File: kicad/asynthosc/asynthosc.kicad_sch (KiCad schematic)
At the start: 0 parts

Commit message: sch: wip
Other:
- sheet Analog_in ports: added CVIN0, CVIN1, CVIN2, CVIN3, TRG0; removed none
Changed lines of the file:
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@@
 	)
 	(sheet
-		(at 95.25 135.89)
+		(at 38.1 123.19)
 		(size 52.07 33.02)
 		(fields_autoplaced yes)
@@
 		)
 		(property "Sheetname" "Analog_in"
-			(at 95.25 135.1784 0)
+			(at 38.1 122.4784 0)
 			(effects
 				(font
@@
 		)
 		(property "Sheetfile" "analog_in.kicad_sch"
-			(at 95.25 169.4946 0)
+			(at 38.1 156.7946 0)
 			(effects
 				(font
@@
 			)
 		)
+		(pin "CVIN1" input
+			(at 90.17 133.35 0)
+			(effects
+				(font
+					(size 1.27 1.27)
+				)
+				(justify right)
+			)
+		)
+		(pin "CVIN2" output
+			(at 90.17 135.89 0)
+			(effects
+				(font
+					(size 1.27 1.27)
+				)
+				(justify right)
+			)
+		)
+		(pin "TRG0" output
+			(at 90.17 142.24 0)
+			(effects
+				(font
+					(size 1.27 1.27)
+				)
+				(justify right)
+			)
+		)
+		(pin "CVIN3" output
+			(at 90.17 138.43 0)
+			(effects
+				(font
+					(size 1.27 1.27)
+				)
+				(justify right)
+			)
+		)
+		(pin "CVIN0" output
+			(at 90.17 130.81 0)
+			(effects
+				(font
+					(size 1.27 1.27)
+				)
+				(justify right)
+			)
+		)

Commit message: sch: rmii side
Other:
- sheet Soc ports: added USB_D_N, USB_D_P, USB_ID, USB_VBUS; removed AIN1
- sheet Supply ports: added USB_ID, USB_VBUS; removed none
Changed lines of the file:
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@@
 	(generator_version "8.0")
 	(paper "A3")
-	(sheet
-		(at 60.96 74.93)
-		(size 50.8 29.21)
+	(wire
+		(pts
+			(xy 111.76 86.36) (xy 127 86.36)
+		)
+		(stroke
+			(width 0)
+			(type default)
+		)
+	)
+	(wire
+		(pts
+			(xy 111.76 81.28) (xy 127 81.28)
+		)
+		(stroke
+			(width 0)
+			(type default)
+		)
+	)
+	(wire
+		(pts
+			(xy 111.76 83.82) (xy 127 83.82)
+		)
+		(stroke
+			(width 0)
+			(type default)
+		)
+	)
+	(wire
+		(pts
+			(xy 111.76 78.74) (xy 127 78.74)
+		)
+		(stroke
+			(width 0)
+			(type default)
+		)
+	)
+	(sheet
+		(at 90.17 74.93)
+		(size 21.59 16.51)
 		(fields_autoplaced yes)
 		(stroke
@@
 		)
 		(property "Sheetname" "Supply"
-			(at 60.96 74.2184 0)
+			(at 90.17 74.2184 0)
 			(effects
 				(font
@@
 		)
 		(property "Sheetfile" "supply.kicad_sch"
-			(at 60.96 104.7246 0)
+			(at 90.17 92.0246 0)
 			(effects
 				(font
@@
 		(pin "USB_DN" input
 			(at 111.76 83.82 0)
+			(effects
+				(font
+					(size 1.27 1.27)
+				)
+				(justify right)
+			)
+		)
+		(pin "USB_VBUS" input
+			(at 111.76 78.74 0)
+			(effects
+				(font
+					(size 1.27 1.27)
+				)
+				(justify right)
+			)
+		)
+		(pin "USB_ID" input
+			(at 111.76 86.36 0)
 			(effects
 				(font
@@
 	)
 	(sheet
-		(at 114.3 176.53)
-		(size 57.15 67.31)
+		(at 127 74.93)
+		(size 49.53 63.5)
 		(fields_autoplaced yes)
 		(stroke
@@
 		)
 		(property "Sheetname" "Soc"
-			(at 114.3 175.8184 0)
+			(at 127 74.2184 0)
 			(effects
 				(font
@@
 		)
 		(property "Sheetfile" "soc.kicad_sch"
-			(at 114.3 244.4246 0)
-			(effects
-				(font
-					(size 1.27 1.27)
-				)
-				(justify left top)
-			)
-		)
-		(pin "AIN1" input
-			(at 114.3 205.74 180)
-			(effects
-				(font
+			(at 127 139.0146 0)
+			(effects
+				(font
+					(size 1.27 1.27)
+				)
+				(justify left top)
+			)
+		)
+		(pin "USB_VBUS" input
+			(at 127 78.74 180)
+			(effects
+				(font
+					(size 1.27 1.27)
+				)
+				(justify left)
+			)
+		)
+		(pin "USB_D_N" bidirectional
+			(at 127 83.82 180)
+			(effects
+				(font
+					(size 1.27 1.27)
+				)
+				(justify left)
+			)
+		)
+		(pin "USB_D_P" bidirectional
+			(at 127 81.28 180)
+			(effects
+				(font
+					(size 1.27 1.27)
+				)
+				(justify left)
+			)
+		)
+		(pin "USB_ID" input
+			(at 127 86.36 180)
+			(effects
+				(font

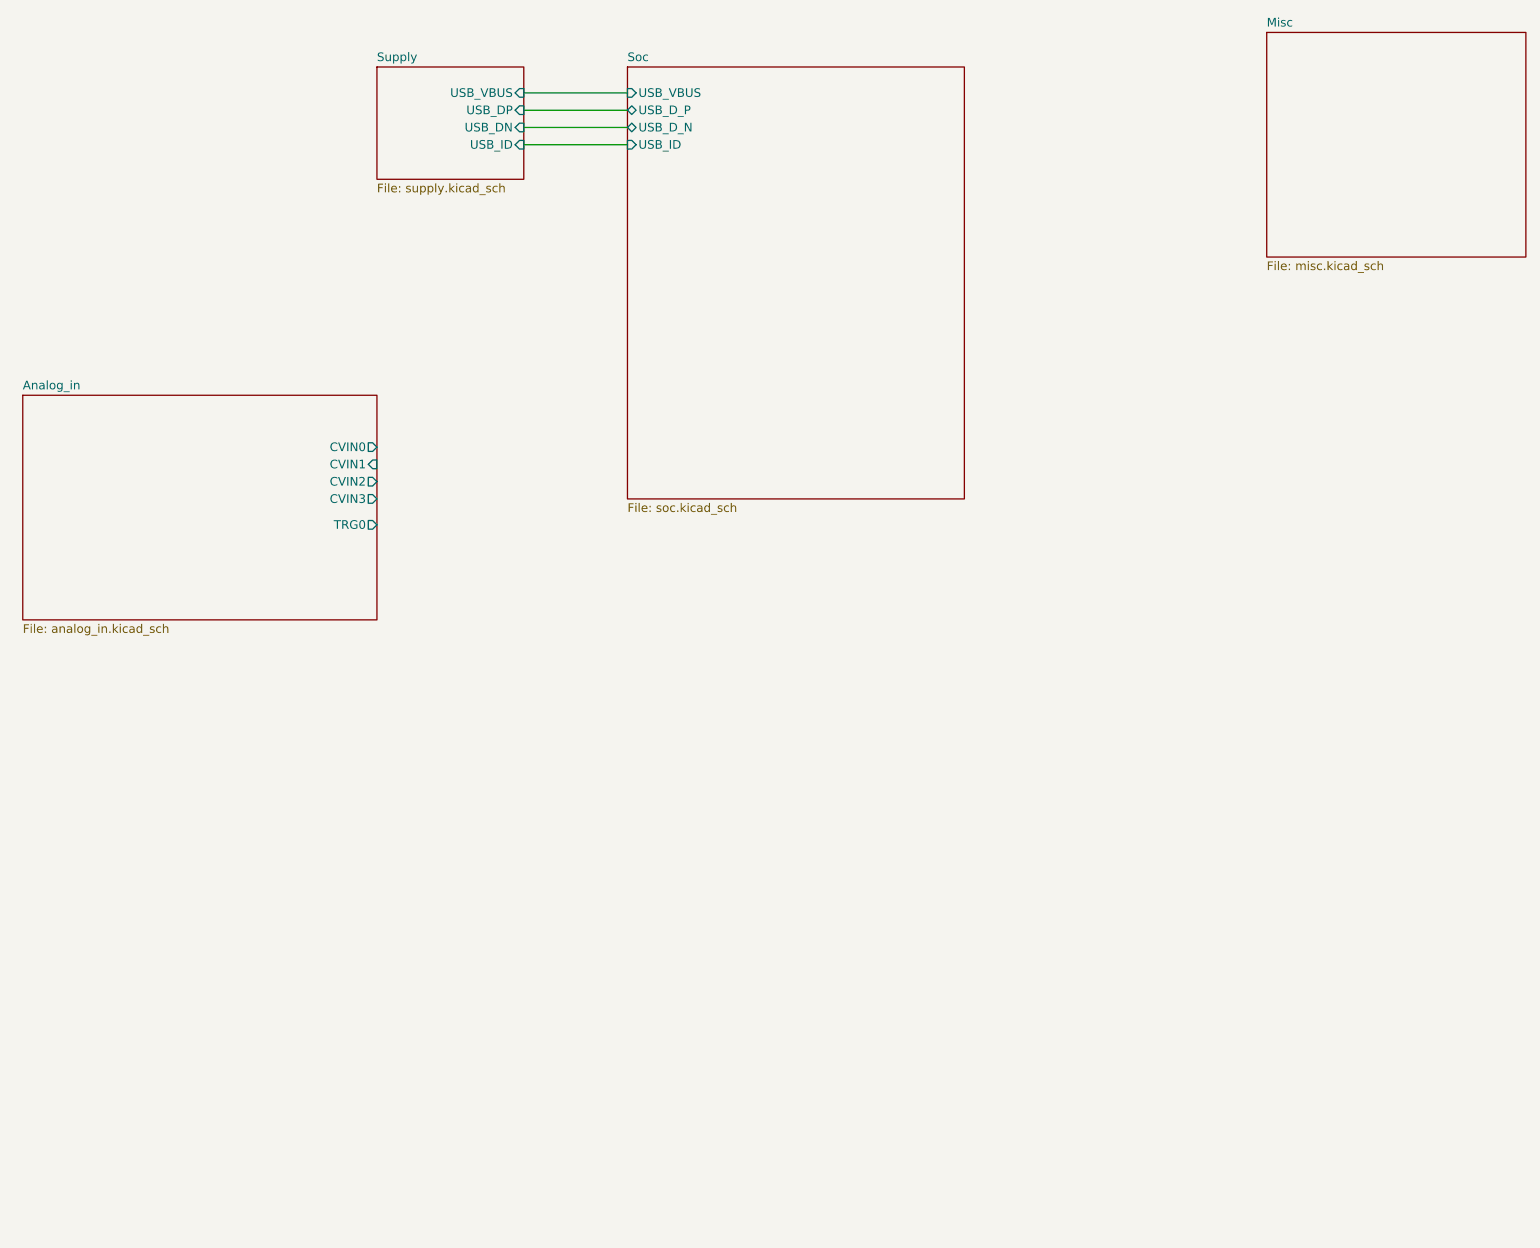
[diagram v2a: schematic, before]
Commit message: sch: top sheet pins input
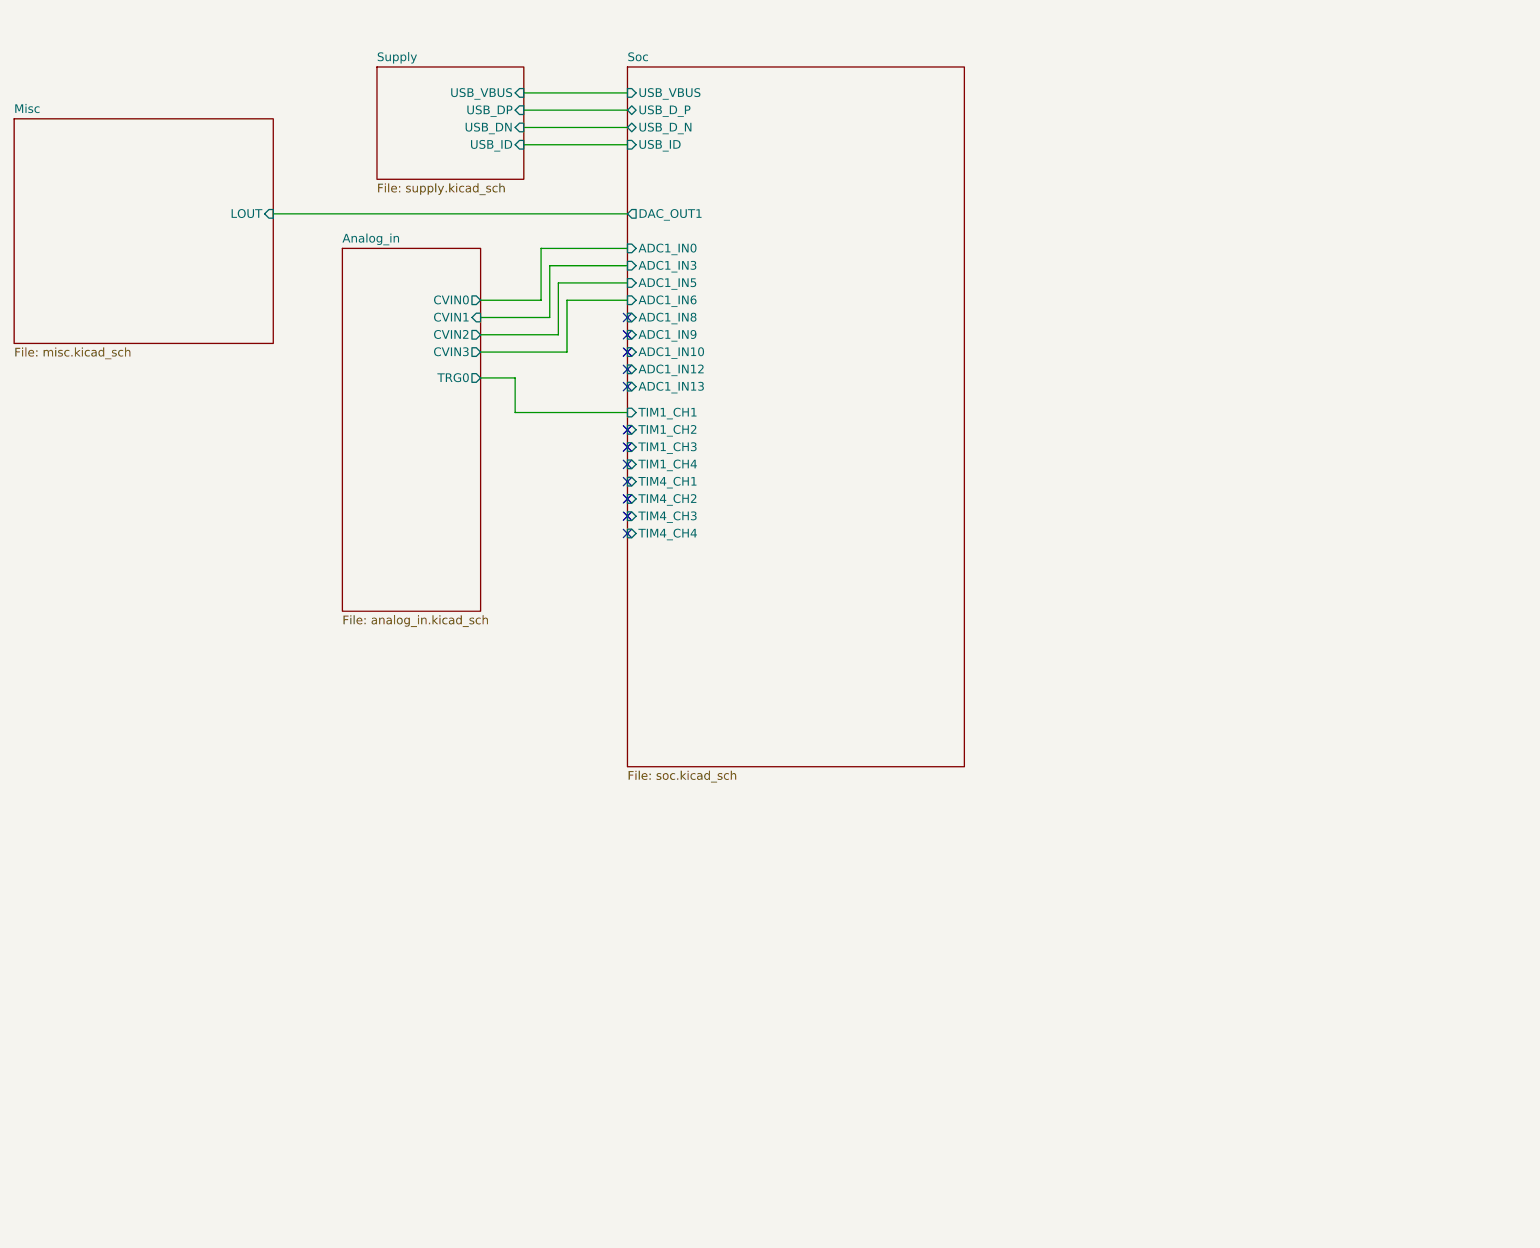
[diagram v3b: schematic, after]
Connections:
- no-connect marks 0 -> 12
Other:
- sheet Misc ports: added LOUT; removed none
- sheet Soc ports: added ADC1_IN0, ADC1_IN10, ADC1_IN12, ADC1_IN13, ADC1_IN3, ADC1_IN5, ADC1_IN6, ADC1_IN8, ADC1_IN9, DAC_OUT1, TIM1_CH1, TIM1_CH2, TIM1_CH3, TIM1_CH4, TIM4_CH1, TIM4_CH2, TIM4_CH3, TIM4_CH4; removed none

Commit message: sch: update and new interface sheet
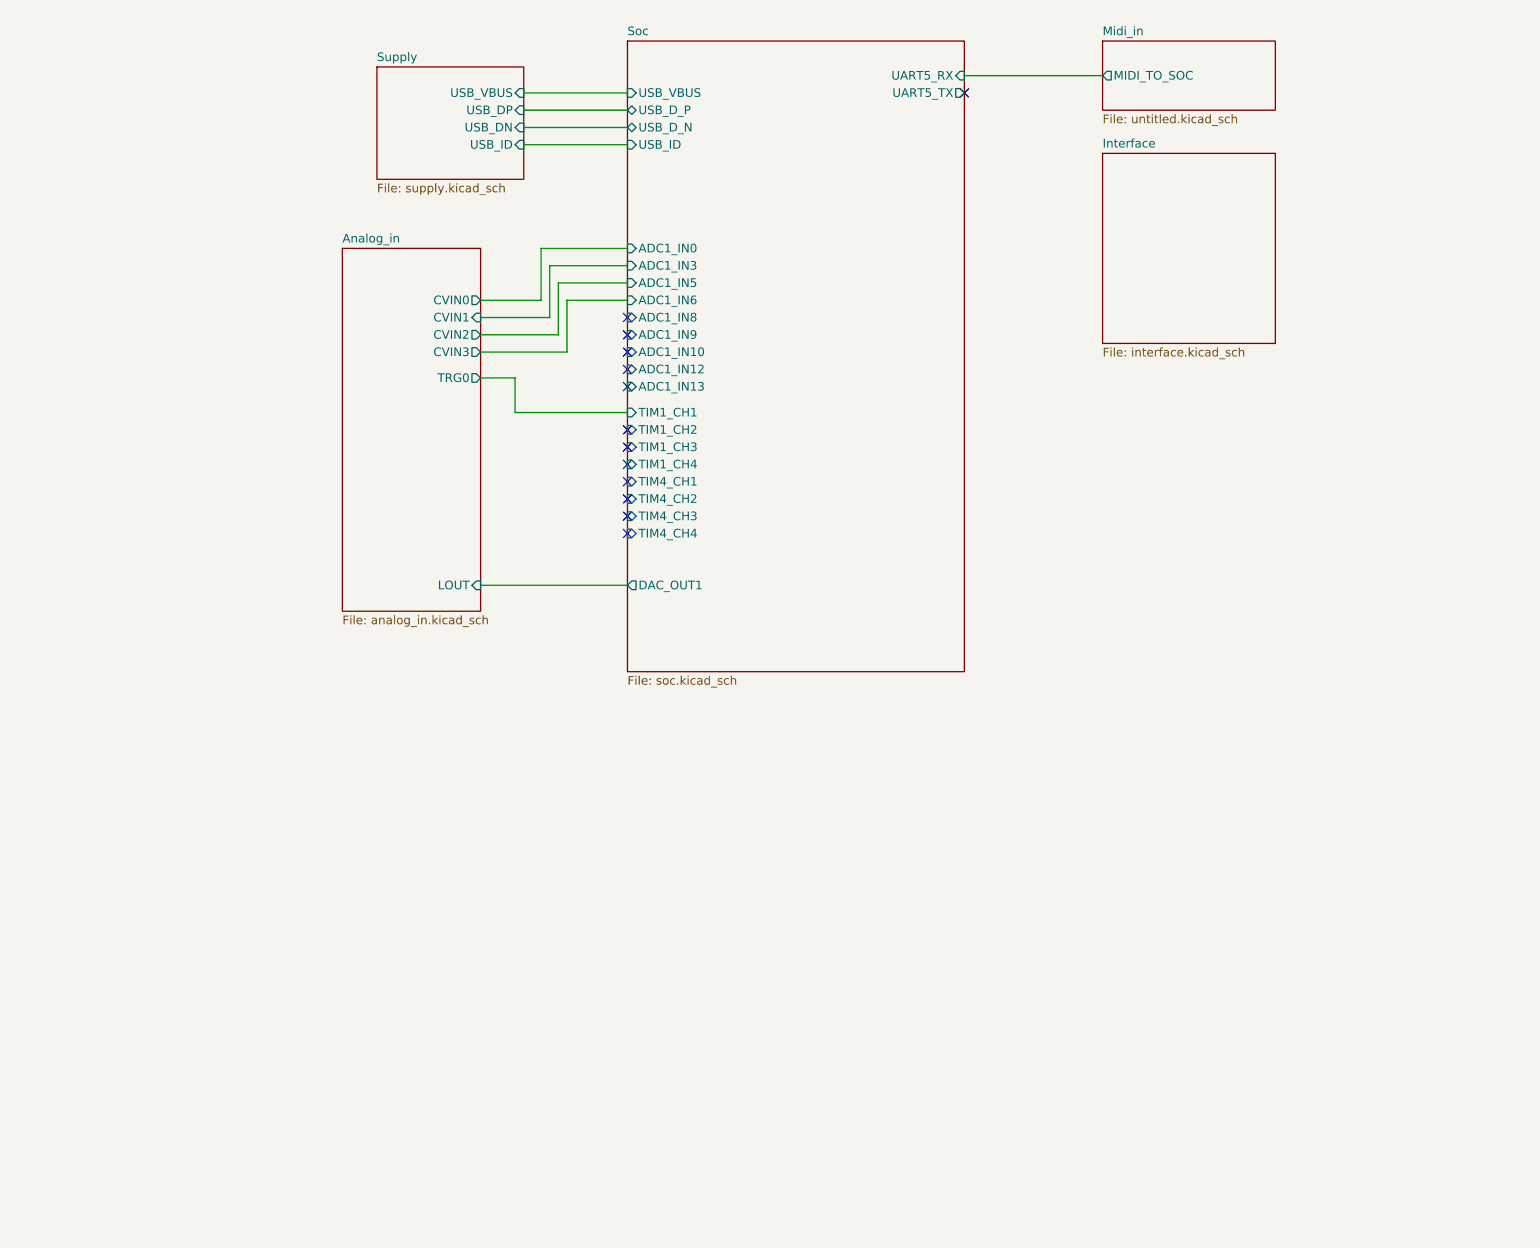
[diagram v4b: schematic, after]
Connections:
- no-connect marks 12 -> 13
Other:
- removed sheet Misc
- added sheet Interface (interface.kicad_sch)
- added sheet Midi_in (untitled.kicad_sch)
- sheet Analog_in ports: added LOUT; removed none
- sheet Soc ports: added UART5_RX, UART5_TX; removed none
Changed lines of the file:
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@@
 		(at 127 128.27)
 	)
-	(wire
-		(pts
-			(xy 74.93 96.52) (xy 127 96.52)
-		)
-		(stroke
-			(width 0)
-			(type default)
-		)
+	(no_connect
+		(at 176.53 78.74)
 	)
 	(wire
@@
 	(wire
 		(pts
+			(xy 176.53 76.2) (xy 196.85 76.2)
+		)
+		(stroke
+			(width 0)
+			(type default)
+		)
+	)
+	(wire
+		(pts
 			(xy 111.76 86.36) (xy 127 86.36)
 		)
@@
 		(pts
 			(xy 105.41 120.65) (xy 110.49 120.65)
+		)
+		(stroke
+			(width 0)
+			(type default)
+		)
+	)
+	(wire
+		(pts
+			(xy 105.41 151.13) (xy 127 151.13)
 		)
 		(stroke
@@
 			)
 		)
+		(pin "LOUT" input
+			(at 105.41 151.13 0)
+			(effects
+				(font
+					(size 1.27 1.27)
+				)
+				(justify right)
+			)
+		)
 		(instances
 			(project "asynthosc"
@@
 	)
 	(sheet
-		(at 36.83 82.55)
-		(size 38.1 33.02)
+		(at 196.85 87.63)
+		(size 25.4 27.94)
 		(fields_autoplaced yes)
 		(stroke
@@
 			(color 0 0 0 0.0000)
 		)
-		(property "Sheetname" "Misc"
-			(at 36.83 81.8384 0)
+		(property "Sheetname" "Interface"
+			(at 196.85 86.9184 0)
 			(effects
 				(font
@@
 			)
 		)
-		(property "Sheetfile" "misc.kicad_sch"
-			(at 36.83 116.1546 0)
+		(property "Sheetfile" "interface.kicad_sch"
+			(at 196.85 116.1546 0)
 			(effects
 				(font
@@
 				)
 				(justify left top)
-			)
-		)
-		(pin "LOUT" input
-			(at 74.93 96.52 0)
-			(effects
-				(font
-					(size 1.27 1.27)
-				)
-				(justify right)
 			)
 		)
@@
 			(project "asynthosc"
 				(path "/d73e377a-a016-415f-8824-91cc6e4907b9"
-					(page "5")
+					(page "12")
 				)
 			)
@@
 	)
 	(sheet
-		(at 127 74.93)
-		(size 49.53 102.87)
+		(at 127 71.12)
+		(size 49.53 92.71)
 		(fields_autoplaced yes)
 		(stroke
@@
 		)
 		(property "Sheetname" "Soc"
-			(at 127 74.2184 0)
+			(at 127 70.4084 0)
 			(effects
 				(font
@@
 		)
 		(property "Sheetfile" "soc.kicad_sch"
-			(at 127 178.3846 0)
+			(at 127 164.4146 0)
 			(effects
 				(font
@@
 		)
 		(pin "DAC_OUT1" output
-			(at 127 96.52 180)
+			(at 127 151.13 180)
 			(effects
 				(font
@@
 				)
 				(justify left)
+			)
+		)
+		(pin "UART5_RX" input
+			(at 176.53 76.2 0)
+			(effects
+				(font
+					(size 1.27 1.27)
+				)
+				(justify right)
+			)
+		)
+		(pin "UART5_TX" output
+			(at 176.53 78.74 0)
+			(effects
+				(font
+					(size 1.27 1.27)
+				)
+				(justify right)
 			)
 		)
@@
 				)
 			)
+		)
+	)
+	(sheet
+		(at 196.85 71.12)
+		(size 25.4 10.16)
+		(fields_autoplaced yes)
+		(stroke
+			(width 0.1524)
+			(type solid)
+		)
+		(fill
+			(color 0 0 0 0.0000)
+		)
+		(property "Sheetname" "Midi_in"
+			(at 196.85 70.4084 0)
+			(effects
+				(font
+					(size 1.27 1.27)
+				)
+				(justify left bottom)
+			)
+		)
+		(property "Sheetfile" "untitled.kicad_sch"
+			(at 196.85 81.8646 0)
+			(effects
+				(font
+					(size 1.27 1.27)
+				)
+				(justify left top)
+			)
+		)
+		(pin "MIDI_TO_SOC" output
+			(at 196.85 76.2 180)
+			(effects
+				(font
+					(size 1.27 1.27)
+				)
+				(justify left)
+			)
+		)
+		(instances
+			(project "asynthosc"
+				(path "/d73e377a-a016-415f-8824-91cc6e4907b9"
+					(page "11")
+				)
+			)
